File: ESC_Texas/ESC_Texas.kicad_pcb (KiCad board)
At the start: 4 copper layers, 118 x 73.2 mm, 156 parts, among them IC1 nRF52840-QFAA-F-R7, IC10 UCC21331CQDRQ1, IC11 LM3480IM3-3.3_NOPB, IC2 UCC21331CQDRQ1, IC3 AD8411AWBRZ, IC4 MC78L05ACHT1G, IC5 AD8411AWBRZ, IC6 MC78L05ACHT1G, IC7 UCC21331CQDRQ1, IC8 AD8411AWBRZ, IC9 MC78L05ACHT1G, J1 Battery-, J10 Conn_01x03_Pin, J11 Conn_01x02_Pin, J13 Conn_01x06_Pin, J14 Conn_01x04_Pin, J15 Conn_01x04_Pin, J16 Conn_01x07_Pin, J2 Conn_01x08_Pin, J3 Motor, J4 Battery+, J5 Conn_01x03_Pin, J6 Conn_01x03_Pin, J7 Conn_01x03_Pin, J8 Conn_01x03_Pin, J9 Conn_01x03_Pin, Q1 IPD100N06S4, Q2 IPD100N06S4, Q3 IPD100N06S4, Q4 IPD100N06S4, Q5 IPD100N06S4, Q6 IPD100N06S4, Y1 CM7V-T1A-32.768kHz, Y2 32MHz

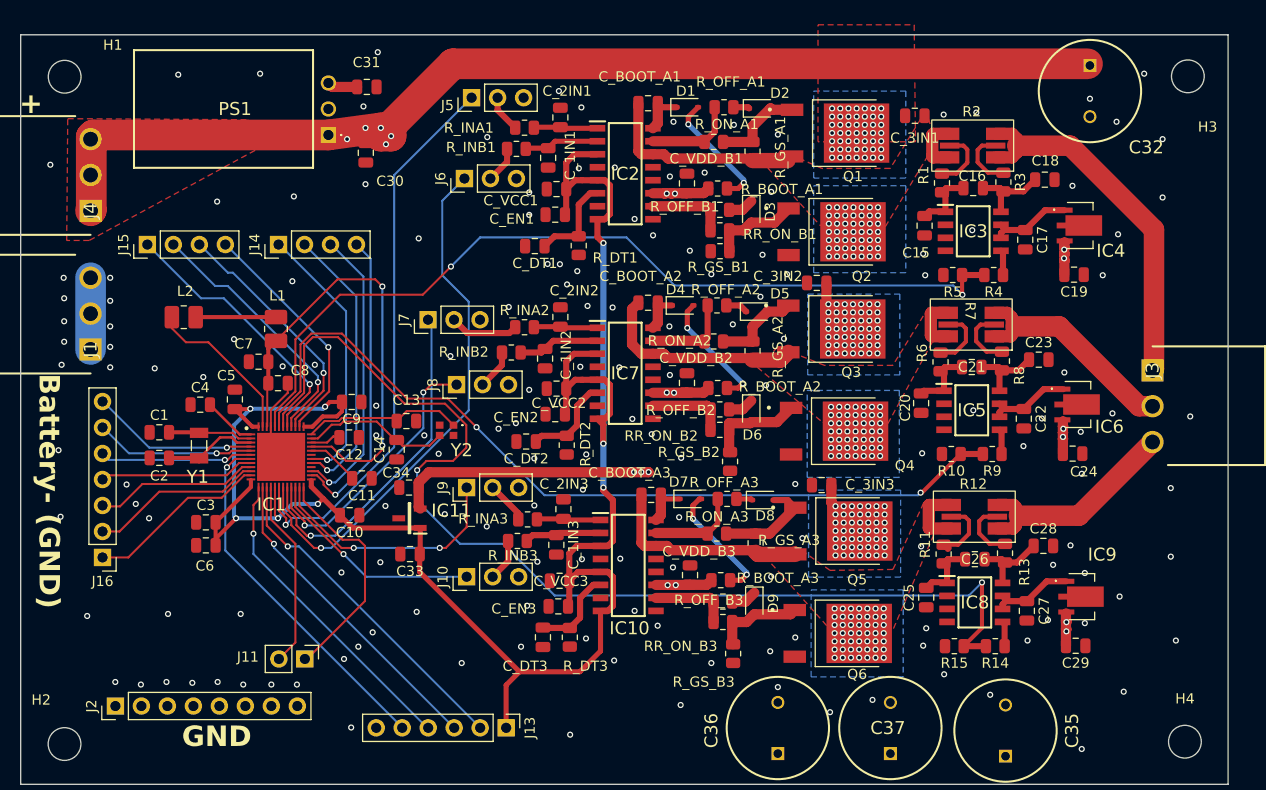
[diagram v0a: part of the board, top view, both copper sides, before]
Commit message: Started with nRF footprint redo
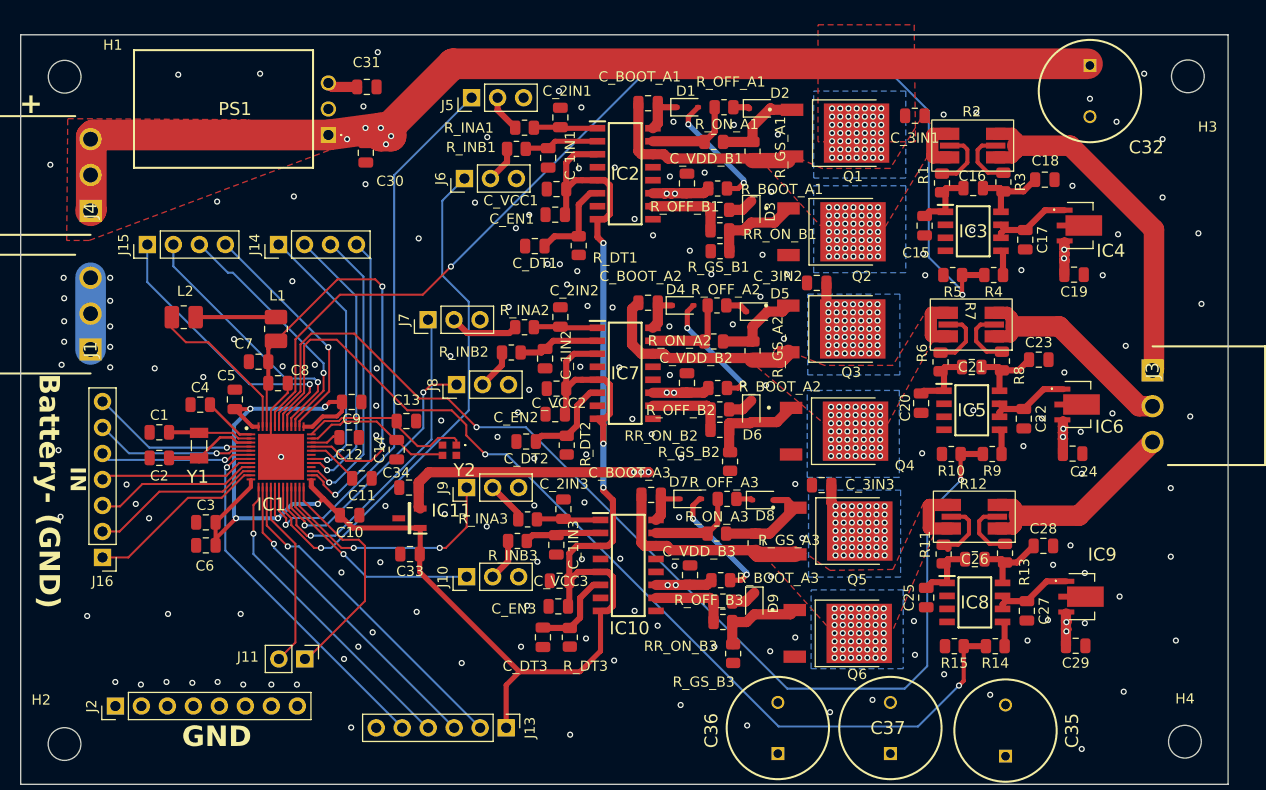
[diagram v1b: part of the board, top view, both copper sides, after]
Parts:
- moved Y2 1.97 mm to (133.9, 114.6)
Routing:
- net P0.30: track 84.3 -> 110.2 mm
- net P0.31: track 85.1 -> 107.9 mm
- net P0.29: track 108.1 -> 97.1 mm
- net P0.28: track 26.6 -> 28.8 mm
- net /XC2: track 15.7 -> 17.1 mm
- net P0.02: track 25.5 -> 26.4 mm
- net GND: vias 162 -> 167
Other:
- board text added: "IN"

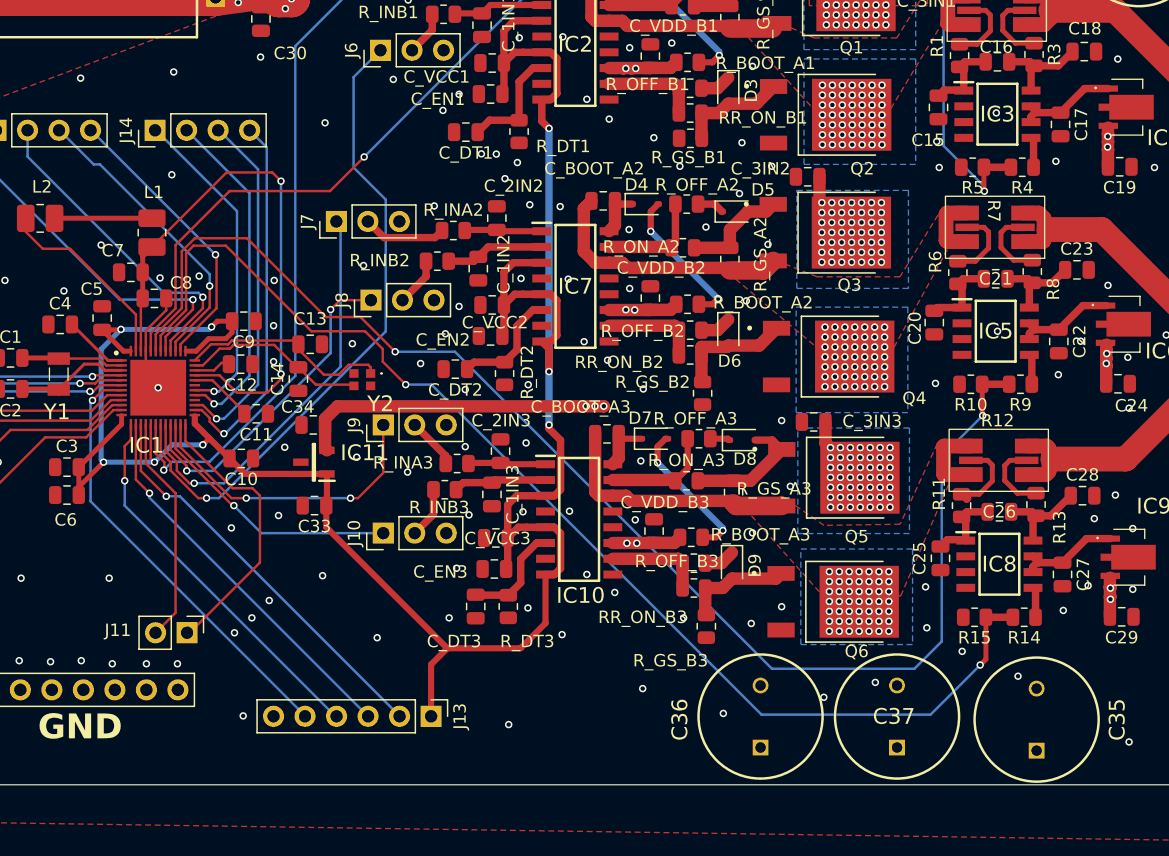
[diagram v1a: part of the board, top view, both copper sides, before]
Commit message: nRF footprint updated
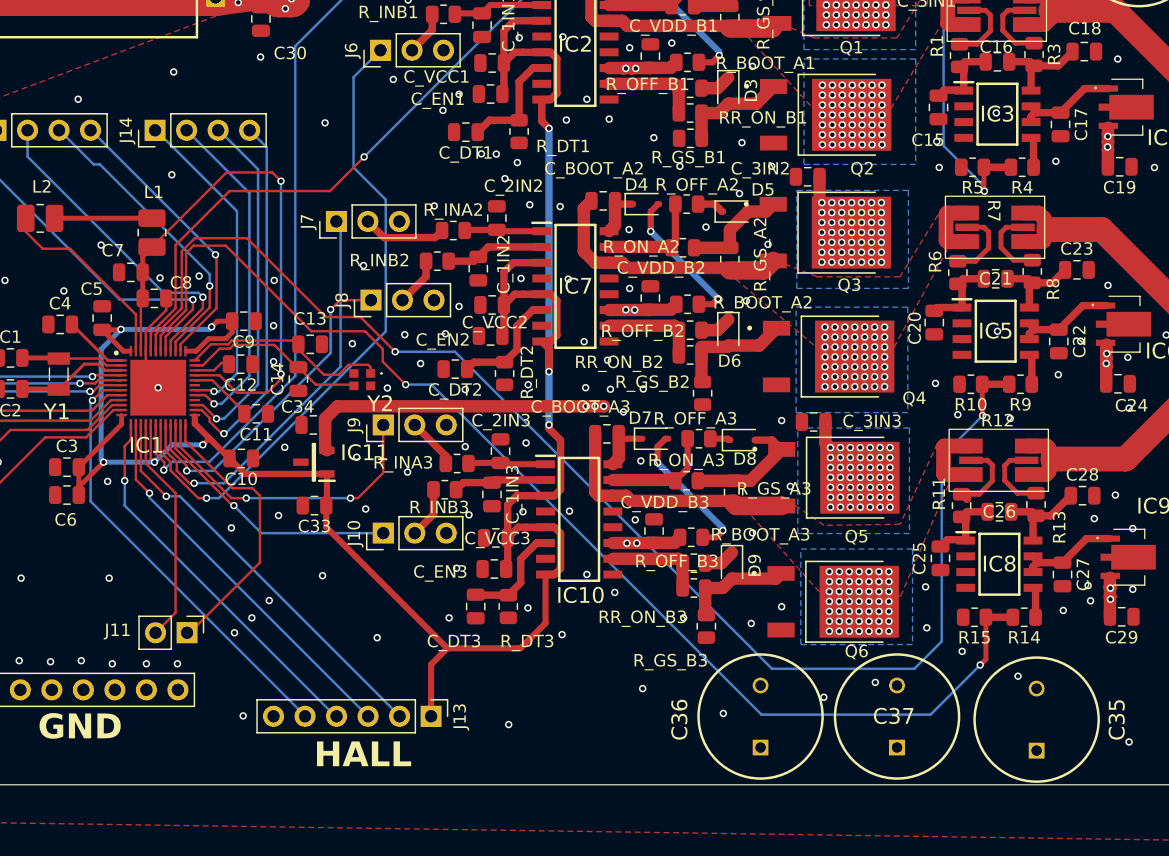
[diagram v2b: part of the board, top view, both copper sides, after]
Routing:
- net GND: vias 167 -> 178
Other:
- board text added: "HALL"

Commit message: Finished
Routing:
- net GND: vias 178 -> 202
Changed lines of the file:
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@@
 	)
 	(via
+		(at 167.4 95.175)
+		(size 0.6)
+		(drill 0.35)
+		(layers "F.Cu" "B.Cu")
+		(free yes)
+		(net 1)
+	)
+	(via
 		(at 196.5 80.25)
 		(size 0.6)
@@
 	)
 	(via
+		(at 167.4 134.425)
+		(size 0.6)
+		(drill 0.35)
+		(layers "F.Cu" "B.Cu")
+		(free yes)
+		(net 1)
+	)
+	(via
 		(at 150.5 106.5)
 		(size 0.6)
@@
 	)
 	(via
+		(at 168 95.85)
+		(size 0.6)
+		(drill 0.35)
+		(layers "F.Cu" "B.Cu")
+		(free yes)
+		(net 1)
+	)
+	(via
 		(at 133.1 111.7)
 		(size 0.6)
@@
 	)
 	(via
+		(at 168.05 135.125)
+		(size 0.6)
+		(drill 0.35)
+		(layers "F.Cu" "B.Cu")
+		(free yes)
+		(net 1)
+	)
+	(via
 		(at 166 83.75)
 		(size 0.6)
@@
 	)
 	(via
+		(at 168.2 114.7)
+		(size 0.6)
+		(drill 0.35)
+		(layers "F.Cu" "B.Cu")
+		(free yes)
+		(net 1)
+	)
+	(via
 		(at 156.55 115.35)
 		(size 0.6)
@@
 	)
 	(via
+		(at 166.75 95.85)
+		(size 0.6)
+		(drill 0.35)
+		(layers "F.Cu" "B.Cu")
+		(free yes)
+		(net 1)
+	)
+	(via
 		(at 195.7 143.8)
 		(size 0.6)
@@
 	)
 	(via
+		(at 166.325 114.7)
+		(size 0.6)
+		(drill 0.35)
+		(layers "F.Cu" "B.Cu")
+		(free yes)
+		(net 1)
+	)
+	(via
+		(at 167.425 135.125)
+		(size 0.6)
+		(drill 0.35)
+		(layers "F.Cu" "B.Cu")
+		(free yes)
+		(net 1)
+	)
+	(via
 		(at 199.4 128.9)
 		(size 0.6)
@@
 	)
 	(via
+		(at 166.8 135.125)
+		(size 0.6)
+		(drill 0.35)
+		(layers "F.Cu" "B.Cu")
+		(free yes)
+		(net 1)
+	)
+	(via
 		(at 120.75 106.25)
 		(size 0.6)
@@
 	)
 	(via
+		(at 166.15 95.175)
+		(size 0.6)
+		(drill 0.35)
+		(layers "F.Cu" "B.Cu")
+		(free yes)
+		(net 1)
+	)
+	(via
 		(at 95.7 114.6)
 		(size 0.6)
@@
 	)
 	(via
+		(at 166.125 95.85)
+		(size 0.6)
+		(drill 0.35)
+		(layers "F.Cu" "B.Cu")
+		(free yes)
+		(net 1)
+	)
+	(via
+		(at 166.95 114.7)
+		(size 0.6)
+		(drill 0.35)
+		(layers "F.Cu" "B.Cu")
+		(free yes)
+		(net 1)
+	)
+	(via
 		(at 207.4 100.3)
 		(size 0.6)
@@
 	)
 	(via
+		(at 168.025 95.175)
+		(size 0.6)
+		(drill 0.35)
+		(layers "F.Cu" "B.Cu")
+		(free yes)
+		(net 1)
+	)
+	(via
 		(at 157.4 95.1)
 		(size 0.6)
@@
 	)
 	(via
+		(at 168.2 115.375)
+		(size 0.6)
+		(drill 0.35)
+		(layers "F.Cu" "B.Cu")
+		(free yes)
+		(net 1)
+	)
+	(via
 		(at 134.175 125.025)
 		(size 0.6)
@@
 	)
 	(via
+		(at 168.675 135.1)
+		(size 0.6)
+		(drill 0.35)
+		(layers "F.Cu" "B.Cu")
+		(free yes)
+		(net 1)
+	)
+	(via
 		(at 100.75 100)
 		(size 0.6)
@@
 	)
 	(via
+		(at 166.775 95.175)
+		(size 0.6)
+		(drill 0.35)
+		(layers "F.Cu" "B.Cu")
+		(free yes)
+		(net 1)
+	)
+	(via
 		(at 164.3 99.6)
 		(size 0.6)
@@
 	)
 	(via
+		(at 166.95 115.375)
+		(size 0.6)
+		(drill 0.35)
+		(layers "F.Cu" "B.Cu")
+		(free yes)
+		(net 1)
+	)
+	(via
 		(at 95.9 121.1)
 		(size 0.6)
@@
 	)
 	(via
+		(at 168.675 134.425)
+		(size 0.6)
+		(drill 0.35)
+		(layers "F.Cu" "B.Cu")
+		(free yes)
+		(net 1)
+	)
+	(via
 		(at 191.8 111.5)
 		(size 0.6)
@@
 	)
 	(via
+		(at 167.575 114.7)
+		(size 0.6)
+		(drill 0.35)
+		(layers "F.Cu" "B.Cu")
+		(free yes)
+		(net 1)
+	)
+	(via
+		(at 167.575 115.375)
+		(size 0.6)
+		(drill 0.35)
+		(layers "F.Cu" "B.Cu")
+		(free yes)
+		(net 1)
+	)
+	(via
+		(at 168.05 134.425)
+		(size 0.6)
+		(drill 0.35)
+		(layers "F.Cu" "B.Cu")
+		(free yes)
+		(net 1)
+	)
+	(via
 		(at 100.75 102.5)
 		(size 0.6)
@@
 	)
 	(via
+		(at 166.325 115.375)
+		(size 0.6)
+		(drill 0.35)
+		(layers "F.Cu" "B.Cu")
+		(free yes)
+		(net 1)
+	)
+	(via
 		(at 116.5 137.5)
 		(size 0.6)
@@
 	)
 	(via
+		(at 167.375 95.85)
+		(size 0.6)
+		(drill 0.35)
+		(layers "F.Cu" "B.Cu")
+		(free yes)
+		(net 1)
+	)
+	(via
 		(at 161.7 82.8)
 		(size 0.6)
@@
 	)
 	(via
+		(at 166.75 134.425)
+		(size 0.6)
+		(drill 0.35)
+		(layers "F.Cu" "B.Cu")
+		(free yes)
+		(net 1)
+	)
+	(via
 		(at 119 137.5)
 		(size 0.6)
@@
 		(min_thickness 0.25)
 		(filled_areas_thickness no)
-		(fill yes
+		(fill
 			(thermal_gap 0.5)
 			(thermal_bridge_width 0.5)
@@
 		(polygon
 			(pts
-				(xy 169.926 73.025) (xy 179.324 73.025) (xy 179.451 84.455) (xy 169.926 84.455)
+				(xy 169.926 75.35) (xy 179.349833 75.35) (xy 179.451 84.455) (xy 169.926 84.455)
 			)
 		)
@@
 		(polygon
 			(pts
-				(xy 83 64) (xy 220 62) (xy 219 152) (xy 83 150)
+				(xy 92 74) (xy 210 74) (xy 210 147.25) (xy 92 147.25)
 			)
 		)
@@
 		(polygon
 			(pts
-				(xy 85.980335 39.248586) (xy 236.48 49.48) (xy 244.39 159.45) (xy 84.480335 160.748586)
+				(xy 92 74) (xy 210 74) (xy 210.025 147.275) (xy 92.01902 147.25)
 			)
 		)

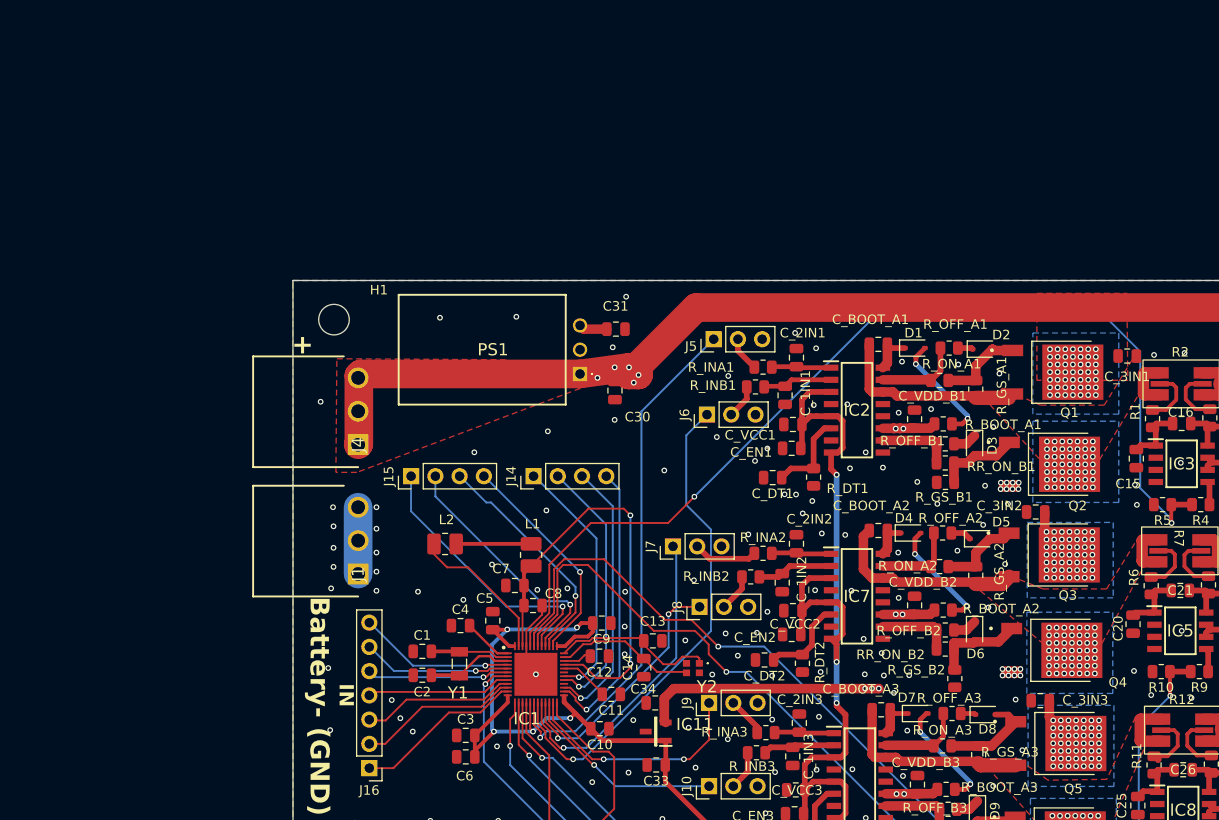
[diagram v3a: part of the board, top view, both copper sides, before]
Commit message: Started adding CAN Module
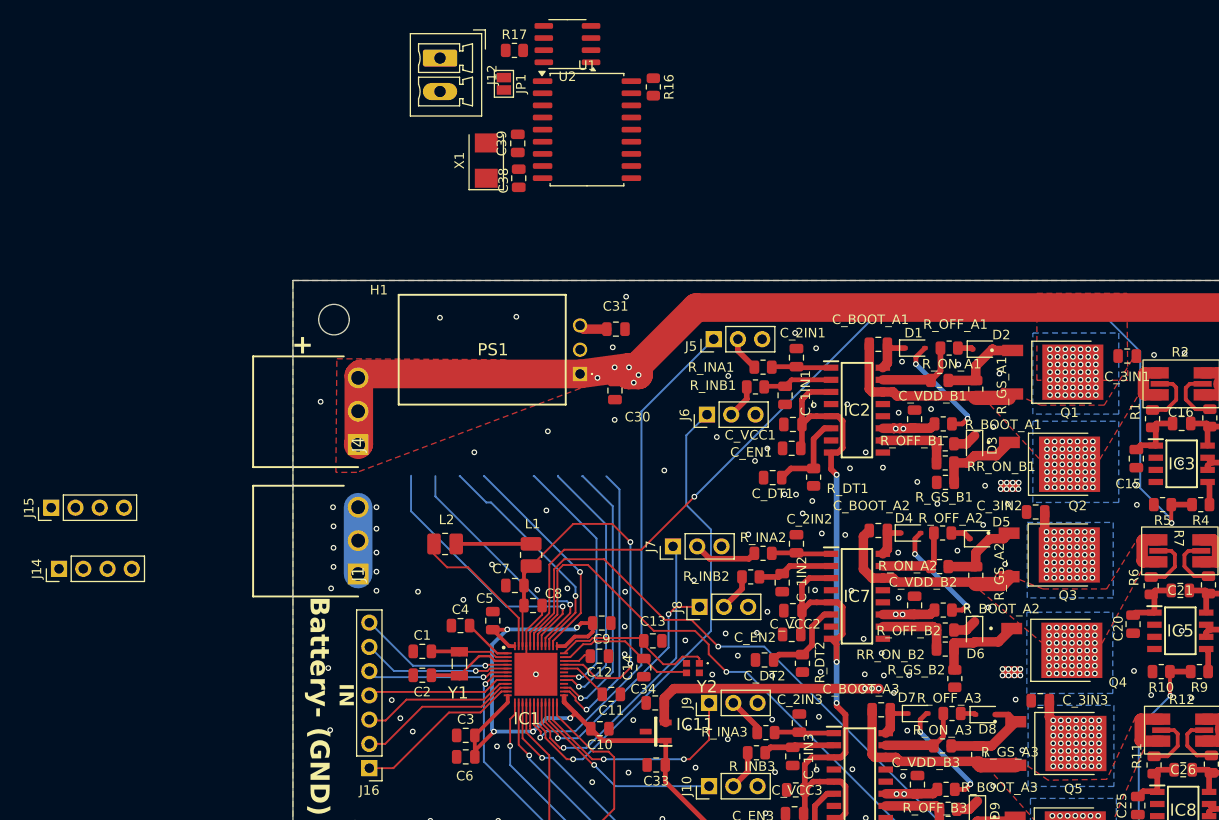
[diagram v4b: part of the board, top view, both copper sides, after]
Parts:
- added C38: 22pF, Capacitor_SMD:C_0805_2012Metric, F.Cu at (115.7, 63.3)
- added C39: 22pF, Capacitor_SMD:C_0805_2012Metric, F.Cu at (115.5, 59.6)
- added J12: Conn_01x02, Connector_Phoenix_MC:PhoenixContact_MCV_1,5_2-G-3.5_1x02_P3.50mm_Vertical, F.Cu at (107.4, 50.7)
- added JP1: SolderJumper_2_Open, Jumper:SolderJumper-2_P1.3mm_Open_Pad1.0x1.5mm, F.Cu at (114.1, 53.4)
- added R16: 10k, Resistor_SMD:R_0805_2012Metric, F.Cu at (129.8, 53.7)
- added R17: 120R, Resistor_SMD:R_0805_2012Metric, F.Cu at (115.2, 49.9)
- added U1: MCP2515-xSO, Package_SO:SOIC-18W_7.5x11.6mm_P1.27mm, F.Cu at (122.8, 58.2)
- added U2: TJA1051T, Package_SO:SOIC-8_3.9x4.9mm_P1.27mm, F.Cu at (120.8, 49.2)
- added X1: C115962, Crystal:Crystal_SMD_5032-2Pin_5.0x3.2mm, F.Cu at (112.2, 61.4)
- moved J14 50.6 mm to (67.5, 104.2)
- moved J15 37.8 mm to (66.7, 97.8)
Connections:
- J15 pad 1: P0.28 -> unconnected-(J15-Pin_1-Pad1)
- J15 pad 2: P0.02 -> unconnected-(J15-Pin_2-Pad2)
- J15 pad 3: P0.03 -> unconnected-(J15-Pin_3-Pad3)
- J15 pad 4: P1.15 -> unconnected-(J15-Pin_4-Pad4)
- J16 pad 4: P1.08 -> unconnected-(J16-Pin_4-Pad4)
- J16 pad 6: P0.05 -> unconnected-(J16-Pin_6-Pad6)
- J16 pad 7: P0.04 -> unconnected-(J16-Pin_7-Pad7)
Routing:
- net DEC6: track 45.9 -> 42.9 mm
